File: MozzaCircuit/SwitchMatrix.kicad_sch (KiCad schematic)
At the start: 94 parts, among them SW13 SW_ChocV2_rev, SW14 SW_ChocV2_rev, SW15 SW_ChocV2_rev, SW21 SW_ChocV2_rev, SW22 SW_ChocV2_rev, SW23 SW_ChocV2_rev, SW24 SW_ChocV2_rev, SW25 SW_ChocV2_rev, SW31 SW_ChocV2_rev, SW32 SW_ChocV2_rev, SW33 SW_ChocV2_rev, SW34 SW_ChocV2_rev, SW35 SW_ChocV2_rev, SW41 SW_ChocV2_rev, SW42 SW_ChocV2_rev, SW43 SW_ChocV2_rev, SW44 SW_ChocV2_rev, SW51 SW_ChocV2_rev, SW52 SW_ChocV2_rev, SW53 SW_ChocV2_rev, SW54 SW_ChocV2_rev, SW61 SW_ChocV2_rev, SW62 SW_ChocV2_rev, SW63 SW_ChocV2_rev, SW64 SW_ChocV2_rev, SW71 SW_ChocV2_rev, SW72 SW_ChocV2_rev, SW73 SW_ChocV2_rev, SW82 SW_ChocV2_rev, SW83 SW_ChocV2_rev, SW84 SW_ChocV2_rev

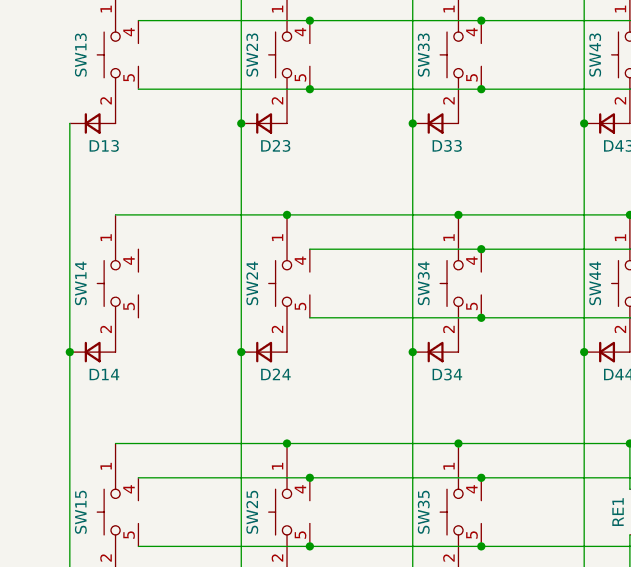
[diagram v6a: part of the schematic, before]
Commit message: footprint circles, fix switch sch
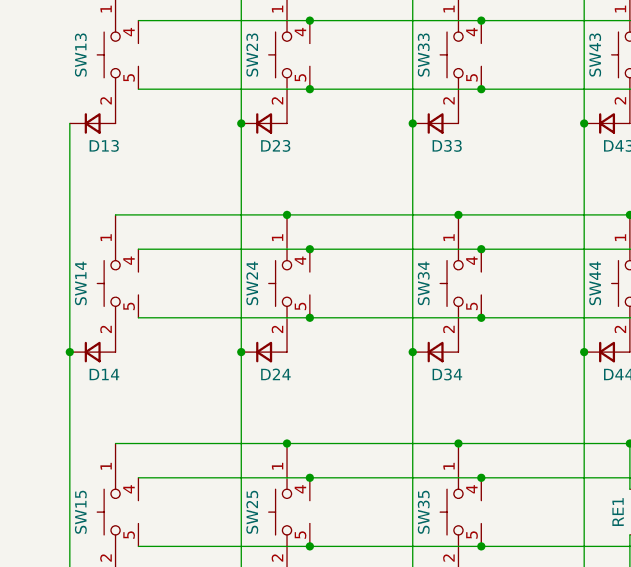
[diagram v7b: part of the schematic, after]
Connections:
- net 5VD: now also SW14.4
- net GNDD: now also SW14.5
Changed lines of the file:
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@@
   (junction (at 26.67 116.84) (diameter 0) (color 0 0 0 0)
   )
+  (junction (at 53.34 113.03) (diameter 0) (color 0 0 0 0)
+  )
   (junction (at 129.54 80.01) (diameter 0) (color 0 0 0 0)
   )
@@
   (junction (at 91.44 36.83) (diameter 0) (color 0 0 0 0)
   )
+  (junction (at 53.34 105.41) (diameter 0) (color 0 0 0 0)
+  )
   (junction (at 72.39 138.43) (diameter 0) (color 0 0 0 0)
   )
@@
     (stroke (width 0) (type default) (color 0 0 0 0))
   )
+  (wire (pts (xy 34.29 105.41) (xy 53.34 105.41))
+    (stroke (width 0) (type default) (color 0 0 0 0))
+  )
   (wire (pts (xy 34.29 80.01) (xy 53.34 80.01))
     (stroke (width 0) (type default) (color 0 0 0 0))
@@
     (stroke (width 0) (type default) (color 0 0 0 0))
   )
+  (wire (pts (xy 34.29 113.03) (xy 53.34 113.03))
+    (stroke (width 0) (type default) (color 0 0 0 0))
+  )

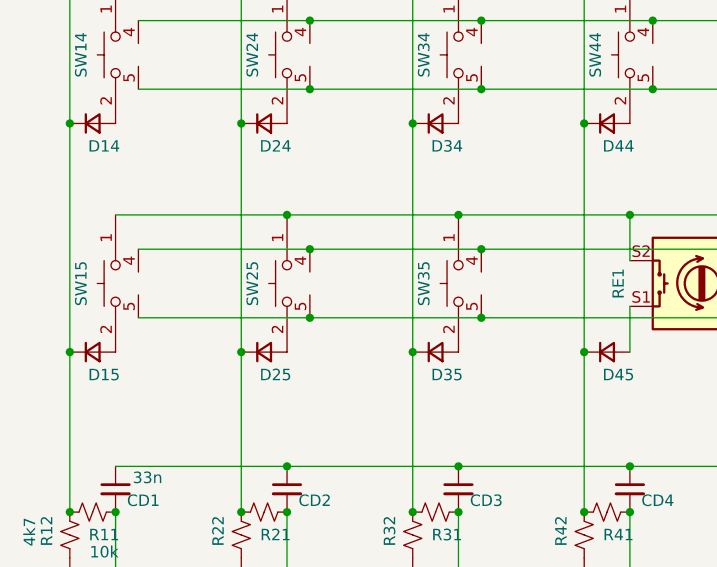
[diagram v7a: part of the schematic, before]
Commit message: column diodes
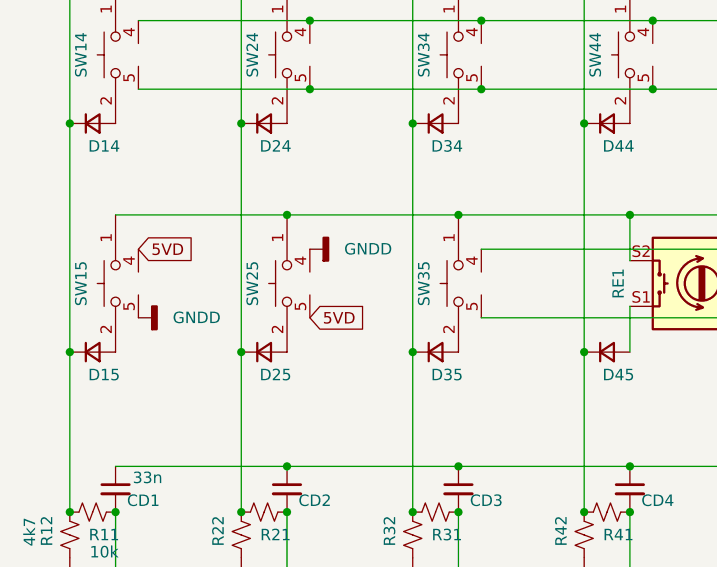
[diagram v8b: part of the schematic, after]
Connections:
- net 5VD: now also SW25.5; no longer SW25.4
- net GNDD: now also SW25.4; no longer SW25.5
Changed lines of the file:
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@@
   (junction (at 45.72 116.84) (diameter 0) (color 0 0 0 0)
   )
-  (junction (at 72.39 130.81) (diameter 0) (color 0 0 0 0)
-  )
   (junction (at 107.95 50.8) (diameter 0) (color 0 0 0 0)
   )
@@
   (junction (at 53.34 105.41) (diameter 0) (color 0 0 0 0)
   )
-  (junction (at 72.39 138.43) (diameter 0) (color 0 0 0 0)
-  )
   (junction (at 110.49 113.03) (diameter 0) (color 0 0 0 0)
   )
@@
   (junction (at 160.02 116.84) (diameter 0) (color 0 0 0 0)
   )
-  (junction (at 53.34 130.81) (diameter 0) (color 0 0 0 0)
-  )
   (junction (at 88.9 76.2) (diameter 0) (color 0 0 0 0)
   )
@@
   (junction (at 146.05 50.8) (diameter 0) (color 0 0 0 0)
   )
-  (junction (at 53.34 138.43) (diameter 0) (color 0 0 0 0)
-  )
   (junction (at 83.82 91.44) (diameter 0) (color 0 0 0 0)
   )
@@
     (stroke (width 0) (type default) (color 0 0 0 0))
   )
-  (wire (pts (xy 34.29 130.81) (xy 53.34 130.81))
-    (stroke (width 0) (type default) (color 0 0 0 0))
-  )
   (wire (pts (xy 45.72 142.24) (xy 45.72 160.02))
     (stroke (width 0) (type default) (color 0 0 0 0))
@@
     (stroke (width 0) (type default) (color 0 0 0 0))
   )
-  (wire (pts (xy 34.29 138.43) (xy 53.34 138.43))
-    (stroke (width 0) (type default) (color 0 0 0 0))
-  )
   (wire (pts (xy 45.72 91.44) (xy 45.72 116.84))
     (stroke (width 0) (type default) (color 0 0 0 0))
@@
     (stroke (width 0) (type default) (color 0 0 0 0))
   )
-  (wire (pts (xy 53.34 138.43) (xy 72.39 138.43))
-    (stroke (width 0) (type default) (color 0 0 0 0))
-  )
   (wire (pts (xy 91.44 87.63) (xy 110.49 87.63))
     (stroke (width 0) (type default) (color 0 0 0 0))
@@
   )
   (wire (pts (xy 110.49 62.23) (xy 129.54 62.23))
-    (stroke (width 0) (type default) (color 0 0 0 0))
-  )
-  (wire (pts (xy 53.34 130.81) (xy 72.39 130.81))
     (stroke (width 0) (type default) (color 0 0 0 0))
   )
@@
     )
   )
+  (global_label "5VD" (shape input) (at 53.34 138.43 0) (fields_autoplaced)
+    (effects (font (size 1.27 1.27)) (justify left))
+    (property "Intersheet References" "${INTERSHEET_REFS}" (id 0) (at 59.3212 138.3506 0)
+      (effects (font (size 1.27 1.27)) (justify left) hide)
+    )
+  )
   (global_label "COL7" (shape input) (at 146.05 167.64 270) (fields_autoplaced)
     (effects (font (size 1.27 1.27)) (justify right))
@@
     (effects (font (size 1.27 1.27)) (justify left))
     (property "Intersheet References" "${INTERSHEET_REFS}" (id 0) (at 191.8245 101.5206 0)
+      (effects (font (size 1.27 1.27)) (justify left) hide)
+    )
+  )
+  (global_label "5VD" (shape input) (at 34.29 130.81 0) (fields_autoplaced)
+    (effects (font (size 1.27 1.27)) (justify left))
+    (property "Intersheet References" "${INTERSHEET_REFS}" (id 0) (at 40.2712 130.7306 0)
       (effects (font (size 1.27 1.27)) (justify left) hide)
     )
@@
     (pin "2")
   )
+  (symbol (lib_id "power:GNDD") (at 53.34 130.81 90) (unit 1)
+    (in_bom yes) (on_board yes) (fields_autoplaced)
+    (property "Reference" "#PWR0138" (id 0) (at 59.69 130.81 0)
+      (effects (font (size 1.27 1.27)) hide)
+    )
+    (property "Value" "GNDD" (id 1) (at 57.15 130.8099 90)
+      (effects (font (size 1.27 1.27)) (justify right))
+    )
+    (property "Footprint" "" (id 2) (at 53.34 130.81 0)
+      (effects (font (size 1.27 1.27)) hide)
+    )
+    (property "Datasheet" "" (id 3) (at 53.34 130.81 0)
+      (effects (font (size 1.27 1.27)) hide)
+    )
+    (pin "1")
+  )
   (symbol (lib_id "Device:D_Small") (at 86.36 91.44 0) (unit 1)
     (in_bom yes) (on_board yes)
@@
     (pin "5")
   )
+  (symbol (lib_id "power:GNDD") (at 34.29 138.43 90) (unit 1)
+    (in_bom yes) (on_board yes) (fields_autoplaced)
+    (property "Reference" "#PWR0139" (id 0) (at 40.64 138.43 0)
+      (effects (font (size 1.27 1.27)) hide)
+    )
+    (property "Value" "GNDD" (id 1) (at 38.1 138.4299 90)
+      (effects (font (size 1.27 1.27)) (justify right))
+    )
+    (property "Footprint" "" (id 2) (at 34.29 138.43 0)
+      (effects (font (size 1.27 1.27)) hide)
+    )
+    (property "Datasheet" "" (id 3) (at 34.29 138.43 0)
+      (effects (font (size 1.27 1.27)) hide)
+    )
+    (pin "1")
+  )
   (symbol (lib_name "SW_ChocV2_rev_12") (lib_id "00_KeyParts:SW_ChocV2_rev") (at 69.85 83.82 90) (mirror x) (unit 1)
